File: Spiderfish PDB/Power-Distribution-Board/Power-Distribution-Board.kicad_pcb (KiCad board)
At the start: 4 copper layers, 100 x 80 mm, 110 parts, among them J1 Conn_01x04_Pin, J2 XT90PB-F, J3 USB_B_Micro, J4 TB002-500-02BE, J5 TB002-500-02BE, J6 TB002-500-02BE, J7 TB002-500-02BE, J8 TB002-500-02BE, J9 TB002-500-02BE, U1 STM32L052K6T6, U10 AOZ2264NQI-11, U2 RT6254BHGJ6F, U3 MIC5504-3.3YM5-TR, U4 USBLC6-2SC6, U5 AOZ2264NQI-11, U6 AOZ2264NQI-11, U7 AOZ2264NQI-11, U8 AOZ2264NQI-11, U9 AOZ2264NQI-11

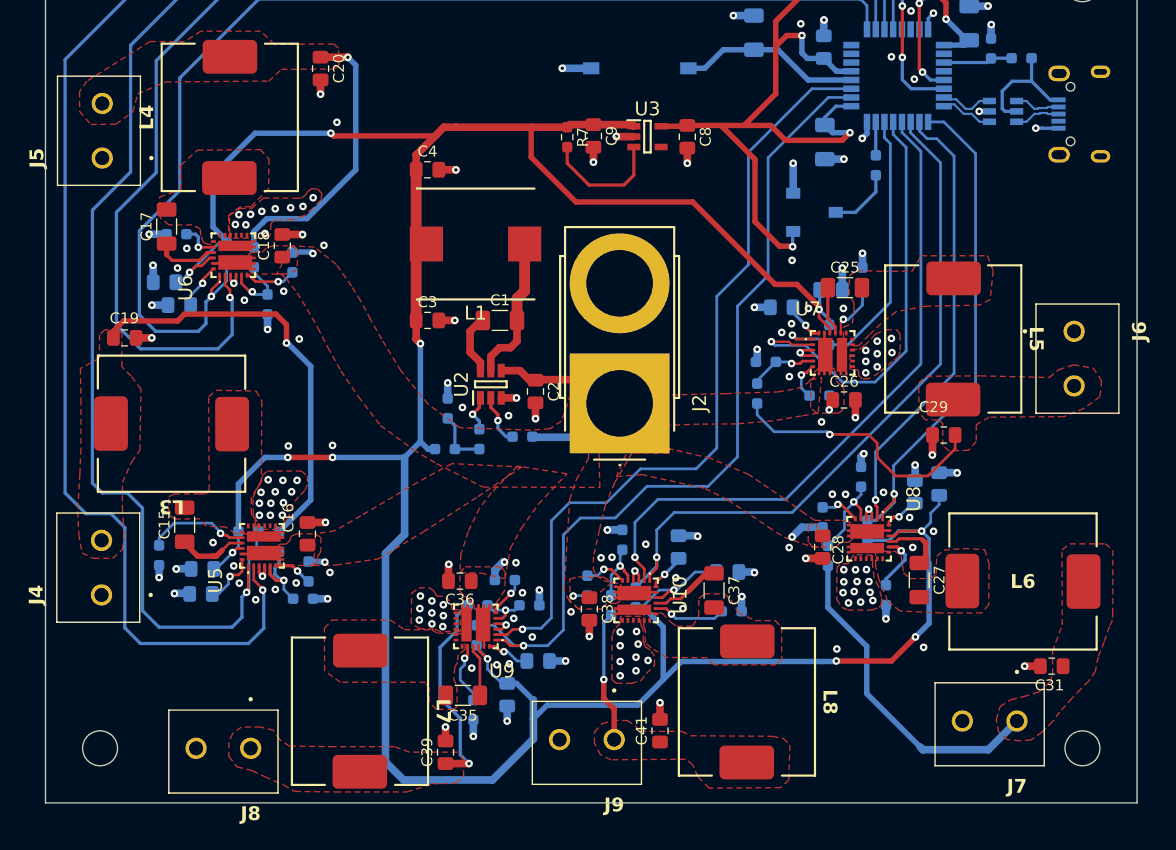
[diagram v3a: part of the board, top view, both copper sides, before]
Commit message: updated silkscreen placement + usb power switch
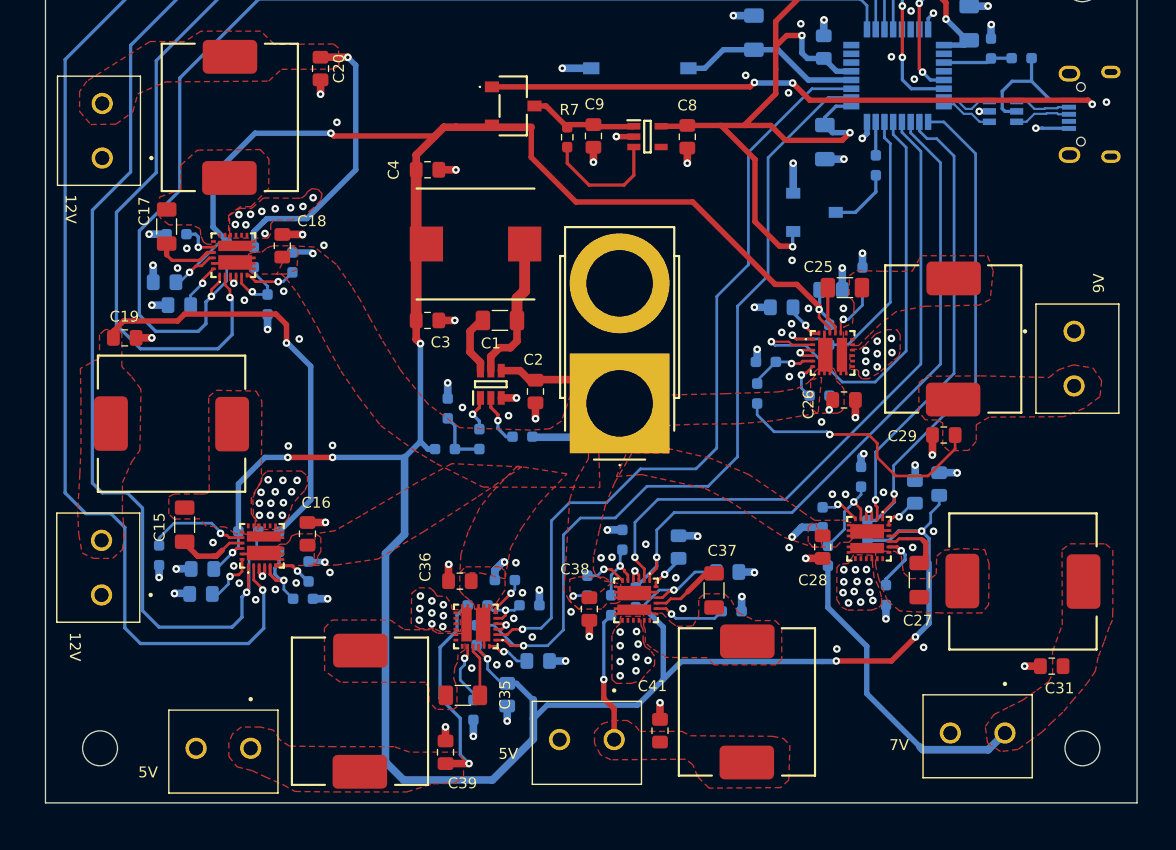
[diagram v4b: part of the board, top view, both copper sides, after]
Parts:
- added S3: CJS-1200TB1, Power_Distribution_Board:CJS1200TB1, F.Cu at (-7.15, -18.9)
- R25: value 374k -> 300k
- R28: value 182k -> 160k
- R31: value 13k -> 15k
- moved J7 1.56 mm to (37.9, 38.6)
- moved J3 1.48 mm to (47.4, -17.9)
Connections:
- net /9V_BST_2 renamed /7V_BST_1
- net /9V_EN_2 renamed /7V_EN_1
- net /9V_FB_2 renamed /7V_FB_1
- net /9V_LX_2 renamed /7V_LX_1
- net /9V_OSC_2 renamed /7V_OSC_1
- net /9V_OUT_2 renamed /7V_OUT_1
- net /9V_PGOOD_2 renamed /7V_PGOOD_1
- net /9V_SS_2 renamed /7V_SS_1
- net /9V_TON_2 renamed /7V_TON_1
- C9 pad 1: +5V -> Net-(S3-COM)
- R7 pad 1: +5V -> Net-(S3-COM)
- U3 pad 1: +5V -> Net-(S3-COM)
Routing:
- net /USB_VBUS: track 11.4 -> 70.6 mm, vias 0 -> 3
- net Net-(S3-COM): track 0.00 -> 10.1 mm
- net +5V: track 294.3 -> 284.7 mm
- net /7V_OUT_1: track 30.2 -> 28.6 mm
- net GND: track 97.0 -> 98.0 mm, vias 172 -> 175
- net /USB_USB_D+: track 4.21 -> 5.15 mm
- net /USB_USB_D-: track 4.21 -> 5.15 mm

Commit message: cleaned up schematic + readme
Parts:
- added G***: LOGO, Power_Distribution_Board:Subbots_Logo_Front, F.Cu at (-13.8, -28.9)
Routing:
- net +14V8: track 45.0 -> 45.5 mm
- net GND: vias 175 -> 176
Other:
- board text added: "UBC Subbots"
